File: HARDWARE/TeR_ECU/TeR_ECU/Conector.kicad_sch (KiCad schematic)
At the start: 1 part, among them IC1 MX34040NF2

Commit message: Revisar y empezar Layout
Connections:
- net +5V: now also IC1.29
- net GND: now also IC1.31, IC1.32; no longer IC1.29
- net LEDs: now reaches IC1.35
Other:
- note added: "Luego mirar a la hora de hacer el layout los pines no solo para la placa sino viendo a dnd van a ir los cables para q no se cruzen."
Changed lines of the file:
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@@
   (junction (at 161.29 83.82) (diameter 0) (color 0 0 0 0)
   )
-  (junction (at 158.75 88.9) (diameter 0) (color 0 0 0 0)
-  )
   (junction (at 161.29 81.28) (diameter 0) (color 0 0 0 0)
   )
@@
   (junction (at 165.1 76.2) (diameter 0) (color 0 0 0 0)
   )
+  (junction (at 161.29 86.36) (diameter 0) (color 0 0 0 0)
+  )
   (junction (at 106.68 96.52) (diameter 0) (color 0 0 0 0)
   )
   (junction (at 102.87 81.28) (diameter 0) (color 0 0 0 0)
   )
+  (junction (at 158.75 93.98) (diameter 0) (color 0 0 0 0)
+  )
+  (junction (at 158.75 91.44) (diameter 0) (color 0 0 0 0)
+  )
   (junction (at 102.87 76.2) (diameter 0) (color 0 0 0 0)
   )
+  (wire (pts (xy 147.32 93.98) (xy 158.75 93.98))
+    (stroke (width 0) (type default))
+  )
   (wire (pts (xy 161.29 78.74) (xy 147.32 78.74))
     (stroke (width 0) (type default))
   )
+  (wire (pts (xy 147.32 101.6) (xy 149.86 101.6))
+    (stroke (width 0) (type default))
+  )
   (wire (pts (xy 165.1 71.12) (xy 147.32 71.12))
     (stroke (width 0) (type default))
@@
     (stroke (width 0) (type default))
   )
-  (wire (pts (xy 158.75 86.36) (xy 158.75 88.9))
-    (stroke (width 0) (type default))
-  )
   (polyline (pts (xy 214.63 12.7) (xy 214.63 38.1))
     (stroke (width 0) (type default))
@@
     (stroke (width 0) (type default))
   )
+  (wire (pts (xy 147.32 91.44) (xy 158.75 91.44))
+    (stroke (width 0) (type default))
+  )
   (wire (pts (xy 119.38 73.66) (xy 124.46 73.66))
     (stroke (width 0) (type default))
   )
-  (wire (pts (xy 147.32 86.36) (xy 158.75 86.36))
+  (wire (pts (xy 147.32 86.36) (xy 161.29 86.36))
     (stroke (width 0) (type default))
   )
@@
     (stroke (width 0) (type default))
   )
+  (wire (pts (xy 158.75 93.98) (xy 158.75 91.44))
+    (stroke (width 0) (type default))
+  )
+  (wire (pts (xy 161.29 88.9) (xy 161.29 86.36))
+    (stroke (width 0) (type default))
+  )
+  (wire (pts (xy 165.1 78.74) (xy 165.1 76.2))
+    (stroke (width 0) (type default))
+  )
+  (wire (pts (xy 147.32 88.9) (xy 158.75 88.9))
+    (stroke (width 0) (type default))
+  )
+  (wire (pts (xy 147.32 73.66) (xy 165.1 73.66))
+    (stroke (width 0) (type default))
+  )
+  (wire (pts (xy 102.87 88.9) (xy 124.46 88.9))
+    (stroke (width 0) (type default))
+  )
+  (wire (pts (xy 102.87 76.2) (xy 124.46 76.2))
+    (stroke (width 0) (type default))
+  )
+  (wire (pts (xy 158.75 95.25) (xy 158.75 93.98))
+    (stroke (width 0) (type default))
+  )
+  (wire (pts (xy 161.29 83.82) (xy 161.29 86.36))
+    (stroke (width 0) (type default))
+  )
+  (wire (pts (xy 161.29 81.28) (xy 161.29 78.74))
+    (stroke (width 0) (type default))
+  )
+  (wire (pts (xy 157.48 68.58) (xy 157.48 66.04))
+    (stroke (width 0) (type default))
+  )
+  (wire (pts (xy 161.29 83.82) (xy 161.29 81.28))
+    (stroke (width 0) (type default))
+  )
+  (wire (pts (xy 119.38 68.58) (xy 124.46 68.58))
+    (stroke (width 0) (type default))
+  )
+  (wire (pts (xy 102.87 83.82) (xy 102.87 81.28))
+    (stroke (width 0) (type default))
+  )
   (wire (pts (xy 158.75 91.44) (xy 158.75 88.9))
     (stroke (width 0) (type default))
   )
-  (wire (pts (xy 165.1 78.74) (xy 165.1 76.2))
-    (stroke (width 0) (type default))
-  )
-  (wire (pts (xy 147.32 88.9) (xy 158.75 88.9))
-    (stroke (width 0) (type default))
-  )
-  (wire (pts (xy 147.32 73.66) (xy 165.1 73.66))
-    (stroke (width 0) (type default))
-  )
-  (wire (pts (xy 102.87 88.9) (xy 124.46 88.9))
-    (stroke (width 0) (type default))
-  )
-  (wire (pts (xy 102.87 76.2) (xy 124.46 76.2))
-    (stroke (width 0) (type default))
-  )
-  (wire (pts (xy 161.29 85.09) (xy 161.29 83.82))
-    (stroke (width 0) (type default))
-  )
-  (wire (pts (xy 161.29 81.28) (xy 161.29 78.74))
-    (stroke (width 0) (type default))
-  )
-  (wire (pts (xy 157.48 68.58) (xy 157.48 66.04))
-    (stroke (width 0) (type default))
-  )
-  (wire (pts (xy 161.29 83.82) (xy 161.29 81.28))
-    (stroke (width 0) (type default))
-  )
-  (wire (pts (xy 119.38 68.58) (xy 124.46 68.58))
-    (stroke (width 0) (type default))
-  )
-  (wire (pts (xy 102.87 83.82) (xy 102.87 81.28))
-    (stroke (width 0) (type default))
-  )
   (wire (pts (xy 102.87 74.93) (xy 102.87 76.2))
     (stroke (width 0) (type default))
@@
     (stroke (width 0) (type default))
   )
+  (text "Alim extra" (at 147.32 93.98 0)
+    (effects (font (size 1.27 1.27)) (justify left bottom))
+  )
   (text "Alim extra" (at 147.32 81.28 0)
     (effects (font (size 1.27 1.27)) (justify left bottom))
@@
   )
   (text "HVD" (at 147.32 78.74 0)
+    (effects (font (size 1.27 1.27)) (justify left bottom))
+  )
+  (text "Alim extra" (at 147.32 91.44 0)
     (effects (font (size 1.27 1.27)) (justify left bottom))
   )
@@
     (effects (font (size 1.27 1.27)) (justify left bottom))
   )
+  (text "Luego mirar a la hora de hacer el layout los \npines no solo para la placa sino viendo a \ndnd van a ir los cables para q no se cruzen."
+    (at 222.25 33.02 0)
+    (effects (font (size 1.27 1.27)) (justify left bottom))
+  )
   (text "Descarga" (at 115.57 86.36 0)
     (effects (font (size 1.27 1.27)) (justify left bottom))
@@
   (hierarchical_label "BL_GND" (shape input) (at 119.38 73.66 180) (fields_autoplaced)
     (effects (font (size 1.27 1.27)) (justify right))
+  )
+  (hierarchical_label "LEDs" (shape input) (at 149.86 101.6 0) (fields_autoplaced)
+    (effects (font (size 1.27 1.27)) (justify left))
   )
   (hierarchical_label "Horn_GND" (shape input) (at 119.38 78.74 180) (fields_autoplaced)
@@
     )
   )
-  (symbol (lib_id "power:GND") (at 158.75 91.44 0) (unit 1)
-    (in_bom yes) (on_board yes) (dnp no) (fields_autoplaced)
-    (property "Reference" "#PWR056" (at 158.75 97.79 0)
-      (effects (font (size 1.27 1.27)) hide)
-    )
-    (property "Value" "GND" (at 158.75 96.52 0)
-      (effects (font (size 1.27 1.27)))
-    )
-    (property "Footprint" "" (at 158.75 91.44 0)
-      (effects (font (size 1.27 1.27)) hide)
-    )
-    (property "Datasheet" "" (at 158.75 91.44 0)
+  (symbol (lib_id "power:GND") (at 158.75 95.25 0) (unit 1)
+    (in_bom yes) (on_board yes) (dnp no) (fields_autoplaced)
+    (property "Reference" "#PWR056" (at 158.75 101.6 0)
+      (effects (font (size 1.27 1.27)) hide)
+    )
+    (property "Value" "GND" (at 158.75 100.33 0)
+      (effects (font (size 1.27 1.27)))
+    )
+    (property "Footprint" "" (at 158.75 95.25 0)
+      (effects (font (size 1.27 1.27)) hide)
+    )
+    (property "Datasheet" "" (at 158.75 95.25 0)
       (effects (font (size 1.27 1.27)) hide)
     )
@@
     )
   )
-  (symbol (lib_id "power:+5V") (at 161.29 85.09 180) (unit 1)
-    (in_bom yes) (on_board yes) (dnp no) (fields_autoplaced)
-    (property "Reference" "#PWR055" (at 161.29 81.28 0)
-      (effects (font (size 1.27 1.27)) hide)
-    )
-    (property "Value" "+5V" (at 161.29 90.17 0)
-      (effects (font (size 1.27 1.27)))
-    )
-    (property "Footprint" "" (at 161.29 85.09 0)
-      (effects (font (size 1.27 1.27)) hide)
-    )
-    (property "Datasheet" "" (at 161.29 85.09 0)
-      (effects (font (size 1.27 1.27)) hide)
-    )
+  (symbol (lib_id "power:+5V") (at 161.29 88.9 180) (unit 1)
+    (in_bom yes) (on_board yes) (dnp no) (fields_autoplaced)
+    (property "Reference" "#PWR055" (at 161.29 85.09 0)
+      (effects (font (size 1.27 1.27)) hide)
+    )
+    (property "Value" "+5V" (at 161.29 93.98 0)
+      (effects (font (size 1.27 1.27)))
+    )
+    (property "Footprint" "" (at 161.29 88.9 0)
+      (effects (font (size 1.27 1.27)) hide)
+    )
+    (property "Datasheet" "" (at 161.29 88.9 0)
+      (effects (font (size 1.27 1.27)) hide)
+    )

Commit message: Revisar y empezar Layout
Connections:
- net GND: now also IC1.14
- net +3.3V: now reaches IC1.15
- net SWCLK: now reaches IC1.16
- net SWDIO: now reaches IC1.17
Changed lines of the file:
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@@
+    (stroke (width 0) (type default))
+  )
+  (wire (pts (xy 118.11 109.22) (xy 124.46 109.22))
     (stroke (width 0) (type default))
   )
@@
     (stroke (width 0) (type default))
   )
+  (wire (pts (xy 114.3 104.14) (xy 124.46 104.14))
+    (stroke (width 0) (type default))
+  )
   (wire (pts (xy 165.1 76.2) (xy 165.1 73.66))
     (stroke (width 0) (type default))
@@
     (stroke (width 0) (type default))
   )
+  (wire (pts (xy 118.11 106.68) (xy 124.46 106.68))
+    (stroke (width 0) (type default))
+  )
   (wire (pts (xy 124.46 86.36) (xy 102.87 86.36))
     (stroke (width 0) (type default))
@@
   )
   (wire (pts (xy 147.32 91.44) (xy 158.75 91.44))
+    (stroke (width 0) (type default))
+  )
+  (wire (pts (xy 119.38 101.6) (xy 124.46 101.6))
     (stroke (width 0) (type default))
   )
@@
     (effects (font (size 1.27 1.27)) (justify left))
   )
+  (hierarchical_label "SWDIO" (shape input) (at 118.11 109.22 180) (fields_autoplaced)
+    (effects (font (size 1.27 1.27)) (justify right))
+  )
   (hierarchical_label "Horn_GND" (shape input) (at 119.38 78.74 180) (fields_autoplaced)
     (effects (font (size 1.27 1.27)) (justify right))
   )
+  (hierarchical_label "SWCLK" (shape input) (at 118.11 106.68 180) (fields_autoplaced)
+    (effects (font (size 1.27 1.27)) (justify right))
+  )
   (symbol (lib_id "power:+24V") (at 106.68 99.06 180) (unit 1)
-    (in_bom yes) (on_board yes) (dnp no) (fields_autoplaced)
+    (in_bom yes) (on_board yes) (dnp no)
     (property "Reference" "#PWR057" (at 106.68 95.25 0)
       (effects (font (size 1.27 1.27)) hide)
     )
-    (property "Value" "+24V" (at 106.68 104.14 0)
+    (property "Value" "+24V" (at 106.68 102.87 0)
       (effects (font (size 1.27 1.27)))
     )
@@
         (path "/84413845-c4f3-4743-bcd2-a67649c90902/e25d0f8a-65a3-47e2-987f-518da8891580"
           (reference "#PWR057") (unit 1)
+        )
+      )
+    )
+  )
+  (symbol (lib_id "power:GND") (at 119.38 101.6 180) (unit 1)
+    (in_bom yes) (on_board yes) (dnp no)
+    (property "Reference" "#PWR063" (at 119.38 95.25 0)
+      (effects (font (size 1.27 1.27)) hide)
+    )
+    (property "Value" "GND" (at 119.38 97.79 0)
+      (effects (font (size 1.27 1.27)))
+    )
+    (property "Footprint" "" (at 119.38 101.6 0)
+      (effects (font (size 1.27 1.27)) hide)
+    )
+    (property "Datasheet" "" (at 119.38 101.6 0)
+      (effects (font (size 1.27 1.27)) hide)
+    )
+    (pin "1")
+    (instances
+      (project "TeR_ECU"
+        (path "/84413845-c4f3-4743-bcd2-a67649c90902/e25d0f8a-65a3-47e2-987f-518da8891580"
+          (reference "#PWR063") (unit 1)
         )
       )
@@
   )
   (symbol (lib_id "power:+12V") (at 157.48 66.04 0) (unit 1)
-    (in_bom yes) (on_board yes) (dnp no) (fields_autoplaced)
+    (in_bom yes) (on_board yes) (dnp no)
     (property "Reference" "#PWR052" (at 157.48 69.85 0)
       (effects (font (size 1.27 1.27)) hide)
     )
-    (property "Value" "+12V" (at 157.48 60.96 0)
+    (property "Value" "+12V" (at 157.48 62.23 0)
       (effects (font (size 1.27 1.27)))
     )
@@
   )
   (symbol (lib_id "power:GND") (at 158.75 95.25 0) (unit 1)
-    (in_bom yes) (on_board yes) (dnp no) (fields_autoplaced)
+    (in_bom yes) (on_board yes) (dnp no)
     (property "Reference" "#PWR056" (at 158.75 101.6 0)
       (effects (font (size 1.27 1.27)) hide)
     )
-    (property "Value" "GND" (at 158.75 100.33 0)
+    (property "Value" "GND" (at 158.75 99.06 0)
       (effects (font (size 1.27 1.27)))
     )
@@
     )
   )
+  (symbol (lib_id "power:+3.3V") (at 114.3 104.14 0) (unit 1)
+    (in_bom yes) (on_board yes) (dnp no)
+    (property "Reference" "#PWR062" (at 114.3 107.95 0)
+      (effects (font (size 1.27 1.27)) hide)
+    )
+    (property "Value" "+3.3V" (at 114.3 100.33 0)
+      (effects (font (size 1.27 1.27)))
+    )
+    (property "Footprint" "" (at 114.3 104.14 0)
+      (effects (font (size 1.27 1.27)) hide)
+    )
+    (property "Datasheet" "" (at 114.3 104.14 0)
+      (effects (font (size 1.27 1.27)) hide)
+    )
+    (pin "1")
+    (instances
+      (project "TeR_ECU"
+        (path "/84413845-c4f3-4743-bcd2-a67649c90902/e25d0f8a-65a3-47e2-987f-518da8891580"
+          (reference "#PWR062") (unit 1)
+        )
+      )
+    )
+  )
   (symbol (lib_id "power:+24V") (at 102.87 74.93 0) (unit 1)
-    (in_bom yes) (on_board yes) (dnp no) (fields_autoplaced)
+    (in_bom yes) (on_board yes) (dnp no)
     (property "Reference" "#PWR051" (at 102.87 78.74 0)
       (effects (font (size 1.27 1.27)) hide)
     )
-    (property "Value" "+24V" (at 102.87 69.85 0)
+    (property "Value" "+24V" (at 102.87 71.12 0)
       (effects (font (size 1.27 1.27)))
     )
@@
   )
   (symbol (lib_id "power:GND") (at 102.87 92.71 0) (unit 1)
-    (in_bom yes) (on_board yes) (dnp no) (fields_autoplaced)
+    (in_bom yes) (on_board yes) (dnp no)
     (property "Reference" "#PWR054" (at 102.87 99.06 0)
       (effects (font (size 1.27 1.27)) hide)
     )
-    (property "Value" "GND" (at 102.87 97.79 0)
+    (property "Value" "GND" (at 102.87 96.52 0)
       (effects (font (size 1.27 1.27)))
     )
@@
   )
   (symbol (lib_id "power:+5V") (at 161.29 88.9 180) (unit 1)
-    (in_bom yes) (on_board yes) (dnp no) (fields_autoplaced)
+    (in_bom yes) (on_board yes) (dnp no)
     (property "Reference" "#PWR055" (at 161.29 85.09 0)
       (effects (font (size 1.27 1.27)) hide)
     )
-    (property "Value" "+5V" (at 161.29 93.98 0)
+    (property "Value" "+5V" (at 161.29 92.71 0)
       (effects (font (size 1.27 1.27)))
     )
@@
   )
   (symbol (lib_id "power:GND") (at 165.1 78.74 0) (unit 1)
-    (in_bom yes) (on_board yes) (dnp no) (fields_autoplaced)
+    (in_bom yes) (on_board yes) (dnp no)
     (property "Reference" "#PWR053" (at 165.1 85.09 0)
       (effects (font (size 1.27 1.27)) hide)
     )
-    (property "Value" "GND" (at 165.1 83.82 0)
-      (effects (font (size 1.27 1.27)))
-    )
+    (property "Value" "GND" (at 165.1 82.55 0)
+      (effects (font (size 1.27 1.27)))
+    )

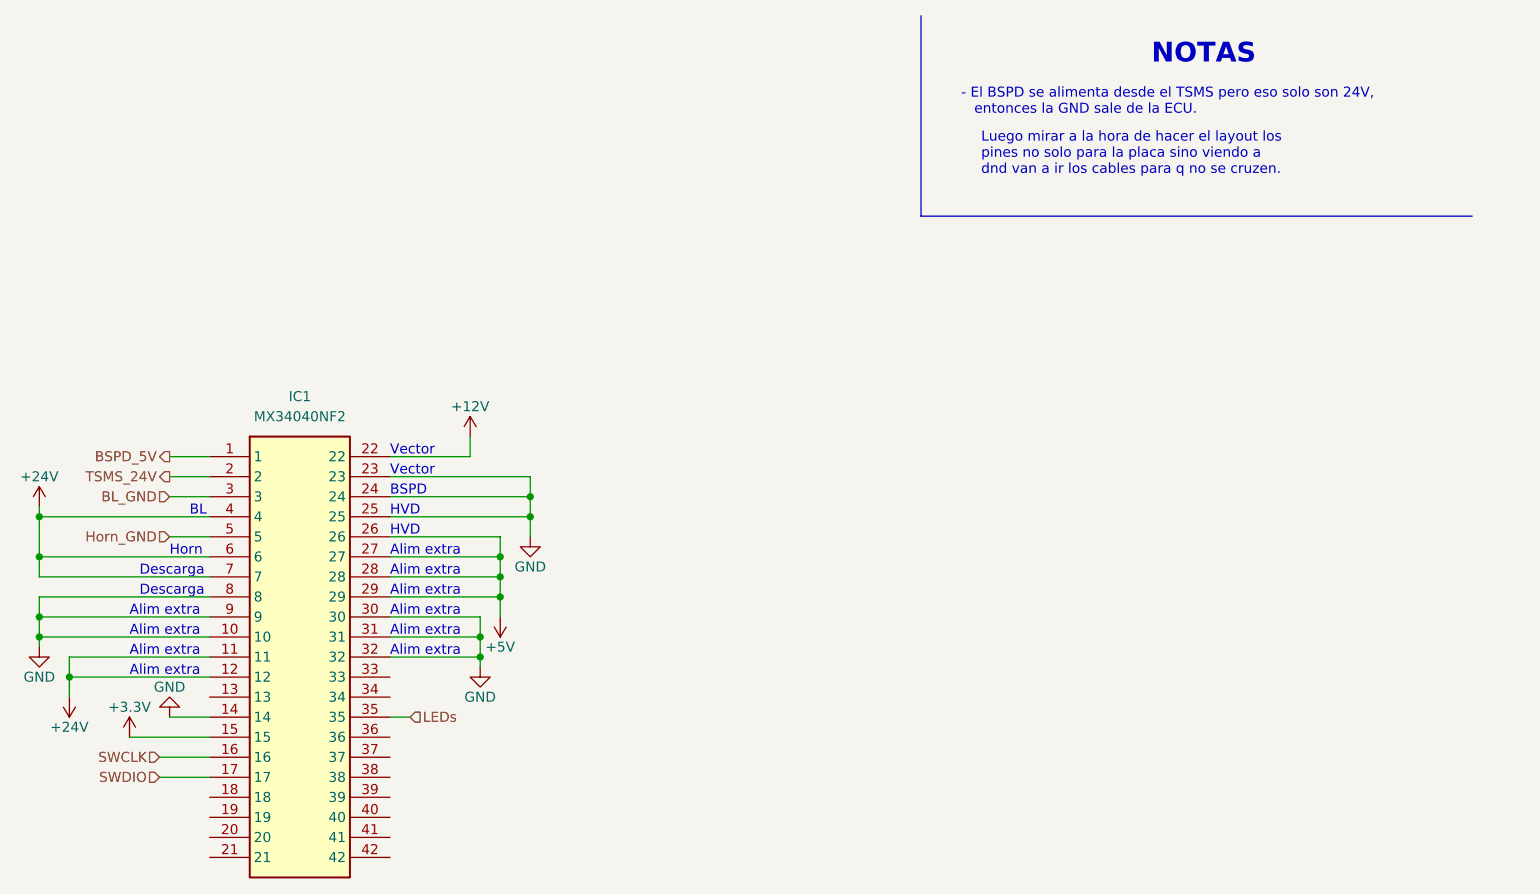
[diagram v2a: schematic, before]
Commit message: añadido alimentacion datalogger
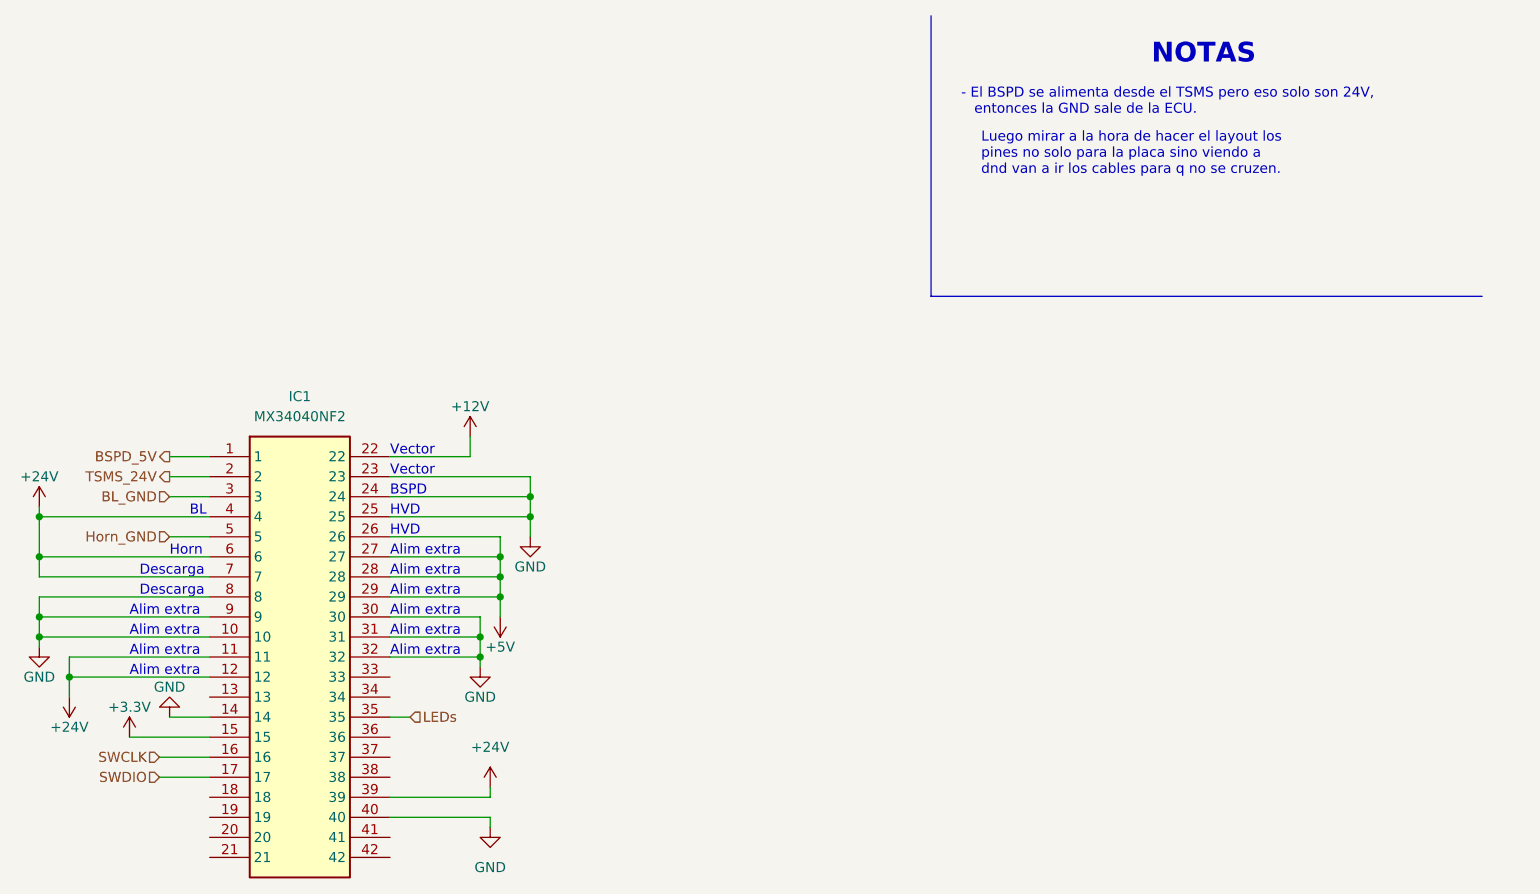
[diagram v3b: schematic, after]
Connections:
- net +24V: now also IC1.39
- net GND: now also IC1.40
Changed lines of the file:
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@@
     (stroke (width 0) (type default))
   )
-  (polyline (pts (xy 214.63 12.7) (xy 214.63 38.1))
+  (wire (pts (xy 160.02 114.3) (xy 160.02 115.57))
+    (stroke (width 0) (type default))
+  )
+  (polyline (pts (xy 215.9 12.7) (xy 215.9 48.26))
     (stroke (width 0) (type default))
   )
@@
     (stroke (width 0) (type default))
   )
+  (wire (pts (xy 147.32 111.76) (xy 160.02 111.76))
+    (stroke (width 0) (type default))
+  )
   (wire (pts (xy 124.46 81.28) (xy 102.87 81.28))
     (stroke (width 0) (type default))
@@
     (stroke (width 0) (type default))
   )
-  (polyline (pts (xy 214.63 38.1) (xy 284.48 38.1))
+  (polyline (pts (xy 215.9 48.26) (xy 285.75 48.26))
     (stroke (width 0) (type default))
   )
@@
     (stroke (width 0) (type default))
   )
+  (wire (pts (xy 160.02 111.76) (xy 160.02 110.49))
+    (stroke (width 0) (type default))
+  )
   (wire (pts (xy 102.87 86.36) (xy 102.87 88.9))
+    (stroke (width 0) (type default))
+  )
+  (wire (pts (xy 147.32 114.3) (xy 160.02 114.3))
     (stroke (width 0) (type default))
   )
@@
   (hierarchical_label "SWCLK" (shape input) (at 118.11 106.68 180) (fields_autoplaced)
     (effects (font (size 1.27 1.27)) (justify right))
+  )
+  (symbol (lib_id "power:GND") (at 160.02 115.57 0) (unit 1)
+    (in_bom yes) (on_board yes) (dnp no) (fields_autoplaced)
+    (property "Reference" "#PWR065" (at 160.02 121.92 0)
+      (effects (font (size 1.27 1.27)) hide)
+    )
+    (property "Value" "GND" (at 160.02 120.65 0)
+      (effects (font (size 1.27 1.27)))
+    )
+    (property "Footprint" "" (at 160.02 115.57 0)
+      (effects (font (size 1.27 1.27)) hide)
+    )
+    (property "Datasheet" "" (at 160.02 115.57 0)
+      (effects (font (size 1.27 1.27)) hide)
+    )
+    (pin "1")
+    (instances
+      (project "TeR_ECU"
+        (path "/84413845-c4f3-4743-bcd2-a67649c90902/e25d0f8a-65a3-47e2-987f-518da8891580"
+          (reference "#PWR065") (unit 1)
+        )
+      )
+    )
   )
   (symbol (lib_id "power:+24V") (at 106.68 99.06 180) (unit 1)
@@
         )
       )
+    )
+  )
+  (symbol (lib_id "power:+24V") (at 160.02 110.49 0) (unit 1)
+    (in_bom yes) (on_board yes) (dnp no) (fields_autoplaced)
+    (property "Reference" "#PWR064" (at 160.02 114.3 0)
+      (effects (font (size 1.27 1.27)) hide)
+    )
+    (property "Value" "+24V" (at 160.02 105.41 0)
+      (effects (font (size 1.27 1.27)))
+    )
+    (property "Footprint" "" (at 160.02 110.49 0)
+      (effects (font (size 1.27 1.27)) hide)
+    )
+    (property "Datasheet" "" (at 160.02 110.49 0)
+      (effects (font (size 1.27 1.27)) hide)
+    )
+    (pin "1")
+    (instances
+      (project "TeR_ECU"
+        (path "/84413845-c4f3-4743-bcd2-a67649c90902/e25d0f8a-65a3-47e2-987f-518da8891580"
+          (reference "#PWR064") (unit 1)
+        )
+      )
